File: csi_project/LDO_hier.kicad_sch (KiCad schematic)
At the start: 8 parts, among them U1 LTC3035EDDBPBF

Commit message: Minor changes
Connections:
- net GND: no longer C15.2, U1.1 (CP)
- new net: C15.2, U1.1 (CP)
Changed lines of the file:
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@@
-	)
-	(junction
-		(at 167.64 102.87)
-		(diameter 0)
-		(color 0 0 0 0)
 	)
 	(junction
@@
 	)
 	(junction
-		(at 102.87 109.22)
-		(diameter 0)
-		(color 0 0 0 0)
-	)
-	(junction
 		(at 80.01 91.44)
-		(diameter 0)
-		(color 0 0 0 0)
-	)
-	(junction
-		(at 167.64 106.68)
 		(diameter 0)
 		(color 0 0 0 0)
@@
 	(wire
 		(pts
+			(xy 184.15 106.68) (xy 184.15 110.49)
+		)
+		(stroke
+			(width 0)
+			(type default)
+		)
+	)
+	(wire
+		(pts
 			(xy 163.83 93.98) (xy 184.15 93.98)
 		)
@@
 	(wire
 		(pts
-			(xy 167.64 102.87) (xy 163.83 102.87)
+			(xy 163.83 102.87) (xy 168.91 102.87)
 		)
 		(stroke
@@
 	(wire
 		(pts
-			(xy 167.64 106.68) (xy 167.64 111.76)
-		)
-		(stroke
-			(width 0)
-			(type default)
-		)
-	)
-	(wire
-		(pts
 			(xy 163.83 99.06) (xy 179.07 99.06)
 		)
@@
 	(wire
 		(pts
-			(xy 93.98 107.95) (xy 93.98 109.22)
-		)
-		(stroke
-			(width 0)
-			(type default)
-		)
-	)
-	(wire
-		(pts
 			(xy 80.01 87.63) (xy 80.01 91.44)
 		)
@@
 	(wire
 		(pts
-			(xy 167.64 106.68) (xy 184.15 106.68)
-		)
-		(stroke
-			(width 0)
-			(type default)
-		)
-	)
-	(wire
-		(pts
 			(xy 58.42 87.63) (xy 80.01 87.63)
 		)
@@
 	(wire
 		(pts
-			(xy 93.98 109.22) (xy 102.87 109.22)
-		)
-		(stroke
-			(width 0)
-			(type default)
-		)
-	)
-	(wire
-		(pts
 			(xy 93.98 99.06) (xy 93.98 100.33)
 		)
@@
 	(wire
 		(pts
-			(xy 167.64 102.87) (xy 168.91 102.87)
-		)
-		(stroke
-			(width 0)
-			(type default)
-		)
-	)
-	(wire
-		(pts
 			(xy 102.87 99.06) (xy 93.98 99.06)
 		)
@@
 	(wire
 		(pts
-			(xy 102.87 109.22) (xy 102.87 113.03)
-		)
-		(stroke
-			(width 0)
-			(type default)
-		)
-	)
-	(wire
-		(pts
-			(xy 167.64 102.87) (xy 167.64 96.52)
+			(xy 102.87 101.6) (xy 102.87 113.03)
+		)
+		(stroke
+			(width 0)
+			(type default)
+		)
+	)
+	(wire
+		(pts
+			(xy 167.64 96.52) (xy 167.64 111.76)
+		)
+		(stroke
+			(width 0)
+			(type default)
+		)
+	)
+	(wire
+		(pts
+			(xy 93.98 107.95) (xy 93.98 113.03)
 		)
 		(stroke
@@
 	(wire
 		(pts
-			(xy 167.64 106.68) (xy 167.64 102.87)
-		)
-		(stroke
-			(width 0)
-			(type default)
-		)
-	)
-	(wire
-		(pts
 			(xy 80.01 91.44) (xy 80.01 95.25)
 		)
@@
 	(wire
 		(pts
-			(xy 102.87 101.6) (xy 102.87 109.22)
-		)
-		(stroke
-			(width 0)
-			(type default)
-		)
-	)
-	(wire
-		(pts
 			(xy 179.07 99.06) (xy 179.07 102.87)
 		)
@@
 		)
 	)
+	(global_label "GND"
+		(shape input)
+		(at 93.98 113.03 270)
+		(fields_autoplaced yes)
+		(effects
+			(font
+				(size 1.27 1.27)
+			)
+			(justify right)
+		)
+		(property "Intersheetrefs" "${INTERSHEET_REFS}"
+			(at 93.98 119.8857 90)
+			(effects
+				(font
+					(size 1.27 1.27)
+				)
+				(justify right)
+				(hide yes)
+			)
+		)
+	)
 	(global_label "1.8V"
 		(shape input)
@@
 			(effects
 				(font
+					(size 1.27 1.27)
+				)
+				(justify right)
+				(hide yes)
+			)
+		)
+	)
+	(global_label "GND"
+		(shape input)
+		(at 184.15 110.49 270)
+		(fields_autoplaced yes)
+		(effects
+			(font
+				(size 1.27 1.27)
+			)
+			(justify right)
+		)
+		(property "Intersheetrefs" "${INTERSHEET_REFS}"
+			(at 184.15 117.3457 90)
+			(effects
+				(font

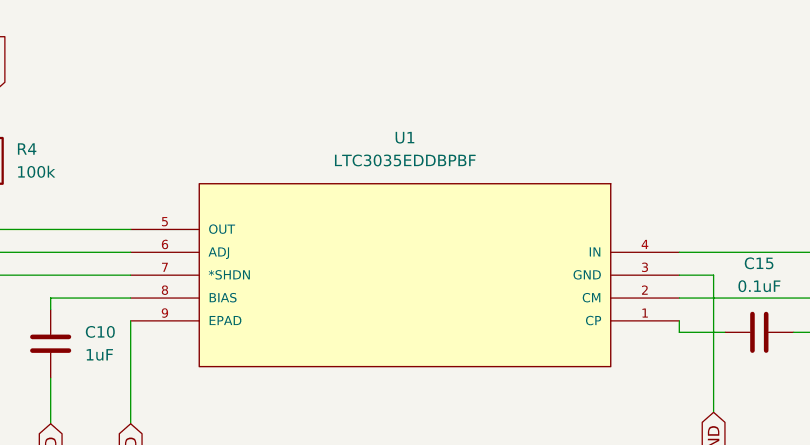
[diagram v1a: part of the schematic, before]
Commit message: Changed file name of schematic pdf, causing git cloning issues.
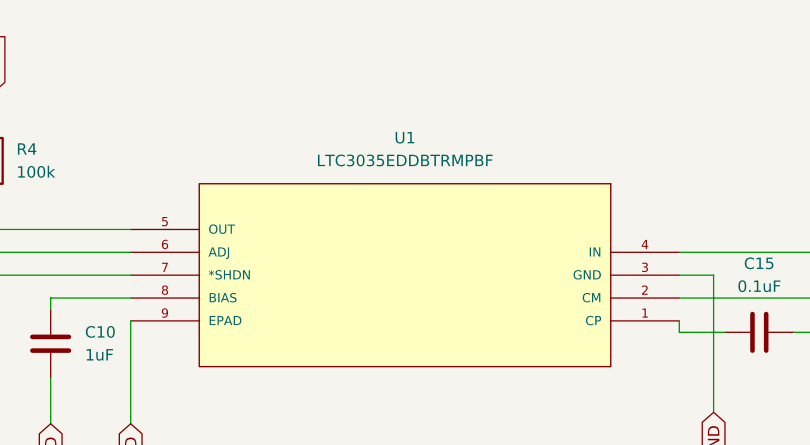
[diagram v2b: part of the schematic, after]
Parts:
- U1: value LTC3035EDDBPBF -> LTC3035EDDBTRMPBF
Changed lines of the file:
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@@
 			)
 		)
-		(property "Value" "LTC3035EDDBPBF"
+		(property "Value" "LTC3035EDDBTRMPBF"
 			(at 133.35 83.82 0)
 			(effects

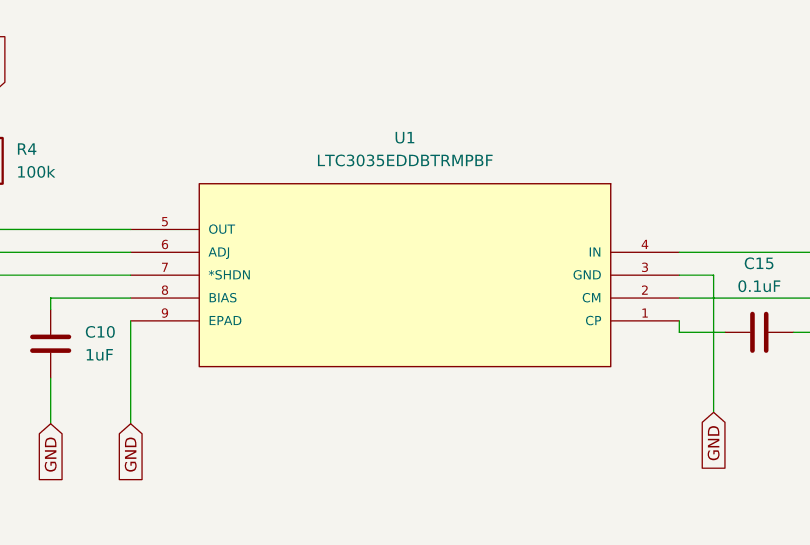
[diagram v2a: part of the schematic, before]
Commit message: Fixed issues with Footprint assignment to main components,
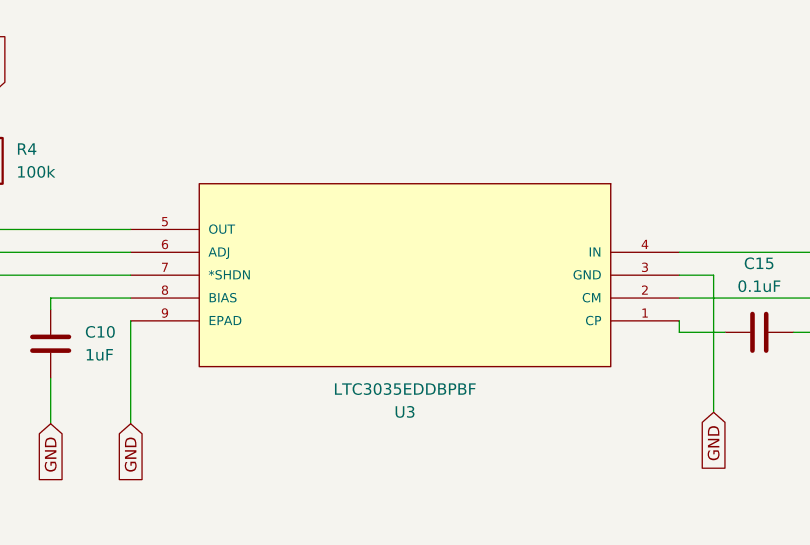
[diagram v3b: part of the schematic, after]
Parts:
- removed U1: LTC3035EDDBTRMPBF, LTC3035EDDBPBF:DFN-8_DDB, symbol LTC3035EDDBPBF:LTC3035EDDBPBF
- added U3: LTC3035EDDBPBF, LTC3035EDDBPBF:LTC3035EDDBPBF, symbol LTC3035EDDBPBF:LTC3035EDDBPBF
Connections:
- net 1.8V: now also U3.5 (OUT)
- net 3.3V: now also U3.4 (IN)
- net GND: now also U3.3 (GND), U3.9 (EPAD)
- net at R5.2, R6.1: now also U3.6 (ADJ)
- net at R4.2: now also U3.7 (*SHDN)
- net at C10.1: now also U3.8 (BIAS)
- net at C15.2: now also U3.1 (CP)
- net at C15.1: now also U3.2 (CM)
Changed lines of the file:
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@@
+	)
+	(symbol
+		(lib_id "LTC3035EDDBPBF:LTC3035EDDBPBF")
+		(at 163.83 101.6 180)
+		(unit 1)
+		(exclude_from_sim no)
+		(in_bom yes)
+		(on_board yes)
+		(dnp no)
+		(property "Reference" "U3"
+			(at 133.35 111.76 0)
+			(effects
+				(font
+					(size 1.27 1.27)
+				)
+			)
+		)
+		(property "Value" "LTC3035EDDBPBF"
+			(at 133.35 109.22 0)
+			(effects
+				(font
+					(size 1.27 1.27)
+				)
+			)
+		)
+		(property "Footprint" "LTC3035EDDBPBF:LTC3035EDDBPBF"
+			(at 163.83 101.6 0)
+			(effects
+				(font
+					(size 1.27 1.27)
+				)
+				(justify bottom)
+				(hide yes)
+			)
+		)
+		(property "Datasheet" ""
+			(at 163.83 101.6 0)
+			(effects
+				(font
+					(size 1.27 1.27)
+				)
+				(hide yes)
+			)
+		)
+		(property "Description" ""
+			(at 163.83 101.6 0)
+			(effects
+				(font
+					(size 1.27 1.27)
+				)
+				(hide yes)
+			)
+		)
+		(property "MF" "Analog Devices"
+			(at 163.83 101.6 0)
+			(effects
+				(font
+					(size 1.27 1.27)
+				)
+				(justify bottom)
+				(hide yes)
+			)
+		)
+		(property "VENDOR" "Linear Technology"
+			(at 163.83 101.6 0)
+			(effects
+				(font
+					(size 1.27 1.27)
+				)
+				(justify bottom)
+				(hide yes)
+			)
+		)
+		(property "Description_1" "\n                        \n                            LTC3035 - 300mA VLDO Linear Regulator with Charge Pump Bias Generator\n                        \n"
+			(at 163.83 101.6 0)
+			(effects
+				(font
+					(size 1.27 1.27)
+				)
+				(justify bottom)
+				(hide yes)
+			)
+		)
+		(property "Package" "DFN-8 Linear Technology"
+			(at 163.83 101.6 0)
+			(effects
+				(font
+					(size 1.27 1.27)
+				)
+				(justify bottom)
+				(hide yes)
+			)
+		)
+		(property "Price" "None"
+			(at 163.83 101.6 0)
+			(effects
+				(font
+					(size 1.27 1.27)
+				)
+				(justify bottom)
+				(hide yes)
+			)
+		)
+		(property "Check_prices" "https://www.snapeda.com/parts/LTC3035EDDB%23PBF/Analog+Devices/view-part/?ref=eda"
+			(at 163.83 101.6 0)
+			(effects
+				(font
+					(size 1.27 1.27)
+				)
+				(justify bottom)
+				(hide yes)
+			)
+		)
+		(property "SnapEDA_Link" "https://www.snapeda.com/parts/LTC3035EDDB%23PBF/Analog+Devices/view-part/?ref=snap"
+			(at 163.83 101.6 0)
+			(effects
+				(font
+					(size 1.27 1.27)
+				)
+				(justify bottom)
+				(hide yes)
+			)
+		)
+		(property "MP" "LTC3035EDDB#PBF"
+			(at 163.83 101.6 0)
+			(effects
+				(font
+					(size 1.27 1.27)
+				)
+				(justify bottom)
+				(hide yes)
+			)
+		)
+		(property "Availability" "In Stock"
+			(at 163.83 101.6 0)
+			(effects
+				(font
+					(size 1.27 1.27)
+				)
+				(justify bottom)
+				(hide yes)
+			)
+		)
+		(property "MANUFACTURER_PART_NUMBER" "ltc3035eddb#pbf"
+			(at 163.83 101.6 0)
+			(effects
+				(font
+					(size 1.27 1.27)
+				)
+				(justify bottom)
+				(hide yes)
+			)
+		)
+		(pin "8"
+		)
+		(pin "3"
+		)
+		(pin "2"
+		)
+		(pin "4"
+		)
+		(pin "9"
+		)
+		(pin "1"
+		)
+		(pin "6"
+		)
+		(pin "5"
+		)
+		(pin "7"
+		)
+		(instances
+			(project ""
+				(path "/d64cee10-711b-40ad-bbb3-ff5a1e2c695b/e845bbdc-135a-413a-b87f-9f2f53546268"
+					(reference "U3")
+					(unit 1)
+				)
+			)
+		)
 	)
 	(symbol
@@
 					(unit 1)
 				)
-			)
-		)
-	)
-	(symbol
-		(lib_id "LTC3035EDDBPBF:LTC3035EDDBPBF")
-		(at 163.83 101.6 180)
-		(unit 1)
-		(exclude_from_sim no)
-		(in_bom yes)
-		(on_board yes)
-		(dnp no)
-		(fields_autoplaced yes)
-		(property "Reference" "U1"
-			(at 133.35 81.28 0)
-			(effects
-				(font
-					(size 1.27 1.27)
-				)
-			)
-		)
-		(property "Value" "LTC3035EDDBTRMPBF"
-			(at 133.35 83.82 0)
-			(effects
-				(font
-					(size 1.27 1.27)
-				)
-			)
-		)
-		(property "Footprint" "LTC3035EDDBPBF:DFN-8_DDB"
-			(at 163.83 101.6 0)
-			(effects
-				(font
-					(size 1.27 1.27)
-				)
-				(justify bottom)
-				(hide yes)
-			)
-		)
-		(property "Datasheet" ""
-			(at 163.83 101.6 0)
-			(effects
-				(font
-					(size 1.27 1.27)
-				)
-				(hide yes)
-			)
-		)
-		(property "Description" ""
-			(at 163.83 101.6 0)
-			(effects
-				(font
-					(size 1.27 1.27)
-				)
-				(hide yes)
-			)
-		)
-		(property "MF" "Analog Devices"
-			(at 163.83 101.6 0)
-			(effects
-				(font
-					(size 1.27 1.27)
-				)
-				(justify bottom)
-				(hide yes)
-			)
-		)
-		(property "VENDOR" "Linear Technology"
-			(at 163.83 101.6 0)
-			(effects
-				(font
-					(size 1.27 1.27)
-				)
-				(justify bottom)
-				(hide yes)
-			)
-		)
-		(property "Description_1" "\n                        \n                            LTC3035 - 300mA VLDO Linear Regulator with Charge Pump Bias Generator\n                        \n"
-			(at 163.83 101.6 0)
-			(effects
-				(font
-					(size 1.27 1.27)
-				)
-				(justify bottom)
-				(hide yes)
-			)
-		)
-		(property "Package" "DFN-8 Linear Technology"
-			(at 163.83 101.6 0)
-			(effects
-				(font
-					(size 1.27 1.27)
-				)
-				(justify bottom)
-				(hide yes)
-			)
-		)
-		(property "Price" "None"
-			(at 163.83 101.6 0)
-			(effects
-				(font
-					(size 1.27 1.27)
-				)
-				(justify bottom)
-				(hide yes)
-			)
-		)
-		(property "Check_prices" "https://www.snapeda.com/parts/LTC3035EDDB%23PBF/Analog+Devices/view-part/?ref=eda"
-			(at 163.83 101.6 0)
-			(effects
-				(font
-					(size 1.27 1.27)
-				)
-				(justify bottom)
-				(hide yes)
-			)
-		)
-		(property "SnapEDA_Link" "https://www.snapeda.com/parts/LTC3035EDDB%23PBF/Analog+Devices/view-part/?ref=snap"
-			(at 163.83 101.6 0)
-			(effects
-				(font
-					(size 1.27 1.27)
-				)
-				(justify bottom)
-				(hide yes)
-			)
-		)
-		(property "MP" "LTC3035EDDB#PBF"
-			(at 163.83 101.6 0)
-			(effects
-				(font
-					(size 1.27 1.27)
-				)
-				(justify bottom)
-				(hide yes)
-			)
-		)
-		(property "Availability" "In Stock"
-			(at 163.83 101.6 0)
-			(effects
-				(font
-					(size 1.27 1.27)
-				)
-				(justify bottom)
-				(hide yes)
-			)
-		)
-		(property "MANUFACTURER_PART_NUMBER" "ltc3035eddb#pbf"
-			(at 163.83 101.6 0)
-			(effects
-				(font
-					(size 1.27 1.27)
-				)
-				(justify bottom)
-				(hide yes)
-			)
-		)
-		(pin "5"
-		)
-		(pin "3"
-		)
-		(pin "4"
-		)
-		(pin "1"
-		)
-		(pin "2"
-		)
-		(pin "8"
-		)
-		(pin "6"
-		)
-		(pin "7"
-		)
-		(pin "9"
-		)
-		(instances
-			(project "csi_project"
-				(path "/d64cee10-711b-40ad-bbb3-ff5a1e2c695b/e845bbdc-135a-413a-b87f-9f2f53546268"
-					(reference "U1")
-					(unit 1)
-				)

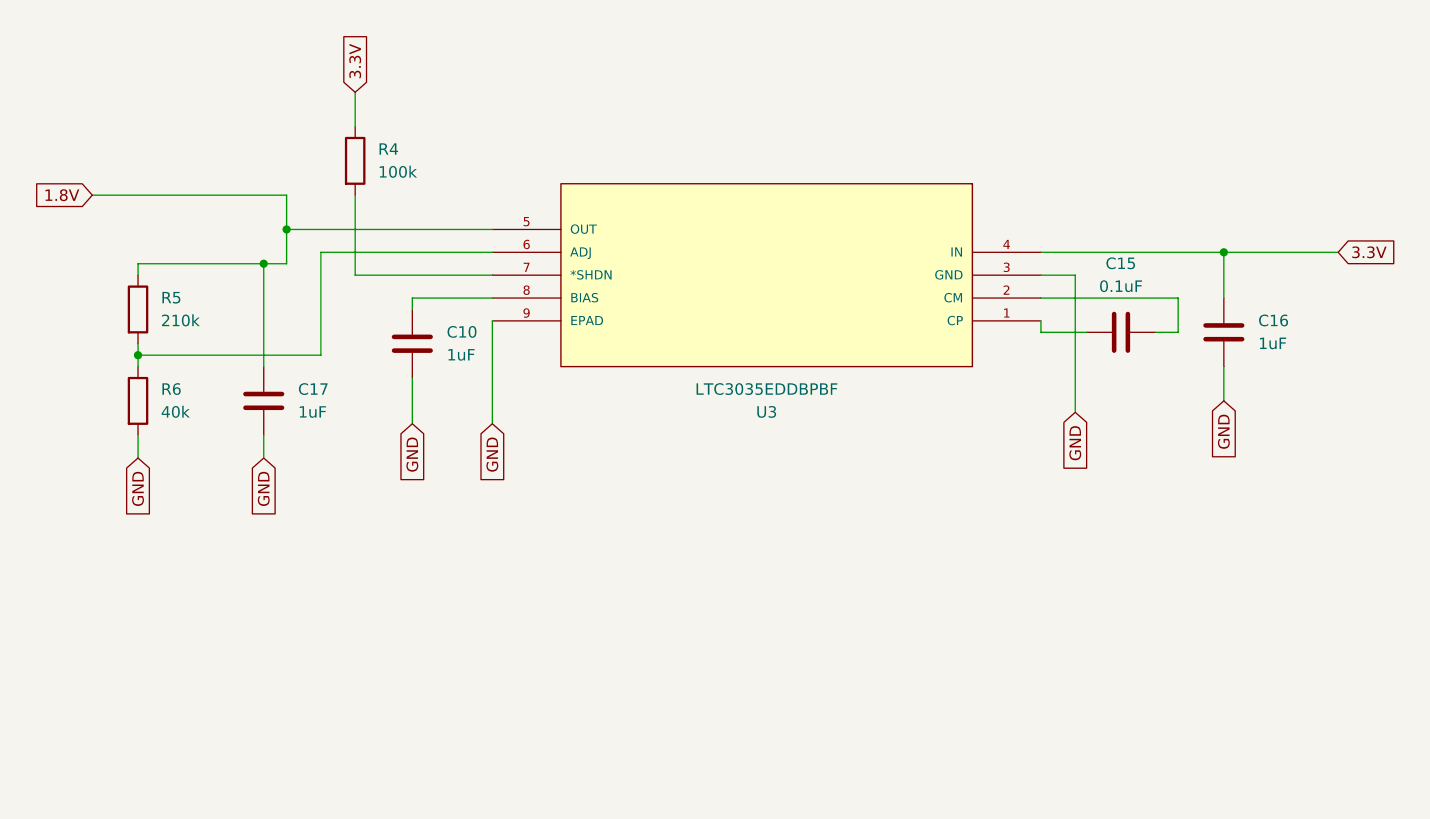
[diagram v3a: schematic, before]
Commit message: Imported custom capacitor and resistor symbols and footprints, and assigned them accordingly.
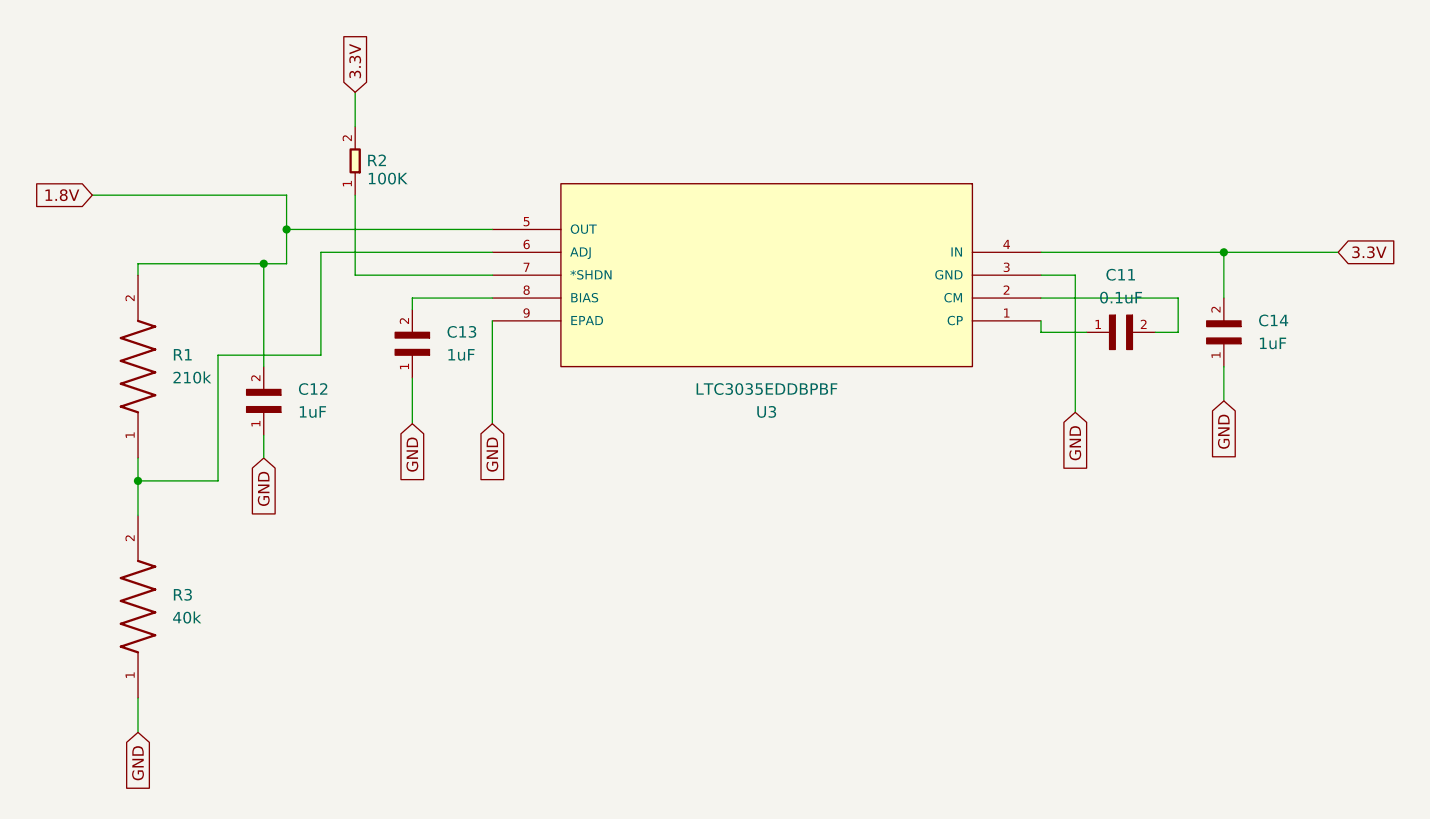
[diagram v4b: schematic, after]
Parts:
- removed C10, C16, C17: 1uF, symbol Device:C
- removed C15: 0.1uF, symbol Device:C
- removed R4: 100k, symbol Device:R
- removed R5: 210k, symbol Device:R
- removed R6: 40k, symbol Device:R
- added C11: 0.1uF, Custom Caps n Res:CL05B104KP5NNNC, symbol Custom Caps n Res:CL05B104KP5NNNC
- added C12, C13, C14: 1uF, Custom Caps n Res:CL10B105KP8NNNC, symbol Custom Caps n Res:CL10B105KP8NNNC
- added R1: 210k, Custom Caps n Res:RC0805FR-07210KL, symbol Custom Caps n Res:RC0805FR-07210KL
- added R2: 100K, Custom Caps n Res:SMD-RES-100K-5_-1_16W_0402_.pretty, symbol Custom Caps n Res:SMD-RES-100K-5_-1_16W_0402_
- added R3: 40k, Custom Caps n Res:CRCW080540K0FKEA, symbol Custom Caps n Res:CRCW080540K0FKEA
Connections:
- net 1.8V: now also C12.2, R1.2
- net 3.3V: now also C14.2, R2.2
- net GND: now also C12.1, C13.1, C14.1, R3.1
- net at U3.6 (ADJ): now also R1.1, R3.2
- net at U3.7 (*SHDN): now also R2.1
- net at U3.1 (CP): now also C11.1
- net at U3.2 (CM): now also C11.2
- net at U3.8 (BIAS): now also C13.2

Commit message: Properly saved changes
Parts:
- removed R1: 210k, Custom Caps n Res:RC0805FR-07210KL, symbol Custom Caps n Res:RC0805FR-07210KL
- removed R3: 40k, Custom Caps n Res:CRCW080540K0FKEA, symbol Custom Caps n Res:CRCW080540K0FKEA
- added R1: 105k, RESC1608X55N:RESC1608X55N, symbol AC0603FR-07105KL:AC0603FR-07105KL
- added R3: 30k, RESC2012X65N:RESC2012X65N, symbol RMCF0805FT30K0:RMCF0805FT30K0
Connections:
- net 1.8V: now also R1.1
- net GND: now also R3.2
- net at U3.6 (ADJ): now also R1.2, R3.1
